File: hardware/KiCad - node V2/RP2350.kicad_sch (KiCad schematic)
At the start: 92 parts, among them J1 Input, J2 Output, J3 USB_C_Receptacle_USB2.0_14P, J4 Screw_Terminal_01x08, SW1 BOOTSEL, U1 RP2350A, U2 THVD1450D, U3 ADXL355BEZ, U4 TPS2121RUXR, U5 USBLC6-2SC6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

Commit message: KiCad: J1 terminal update
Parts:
- removed J1: Input, TerminalBlock_RND:TerminalBlock_RND_205-00278_1x04_P5.00mm_Vertical, symbol Connector:Screw_Terminal_01x04
- removed J2: Output, symbol Connector:Screw_Terminal_01x04
- added C_SHIELD: 10nF, Capacitor_SMD:C_0805_2012Metric, symbol Device:C_Small
- added J1: JST-XH-10, footprints:CONN-TH_10P-P2.50_B10B-XH-A-LF-SN, symbol Connector_Generic:Conn_01x10
- added R_SHIELD: 1M, Resistor_SMD:R_0603_1608Metric, symbol Device:R_Small
- added R_SHIELD_0R: 0R DNP, Resistor_SMD:R_0805_2012Metric, symbol Device:R_Small
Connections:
- net GND: now also C_SHIELD.1, J1.3 (GND_IN), J1.4 (GND_OUT), R_SHIELD.1, R_SHIELD_0R.1
- net at D4.2 (A2), R21.1, U2.6 (A): now also J1.5 (A_IN), J1.7 (A_OUT)
- net at D4.1 (A1), JP1.1 (A), U2.7 (B): now also J1.6 (B_IN), J1.8 (B_OUT)
- net at F1.1: now also J1.1 (12VIN), J1.2 (12VOUT)
- new net: C_SHIELD.2, J1.10 (SH_OUT), J1.9 (SH_IN), R_SHIELD.2, R_SHIELD_0R.2

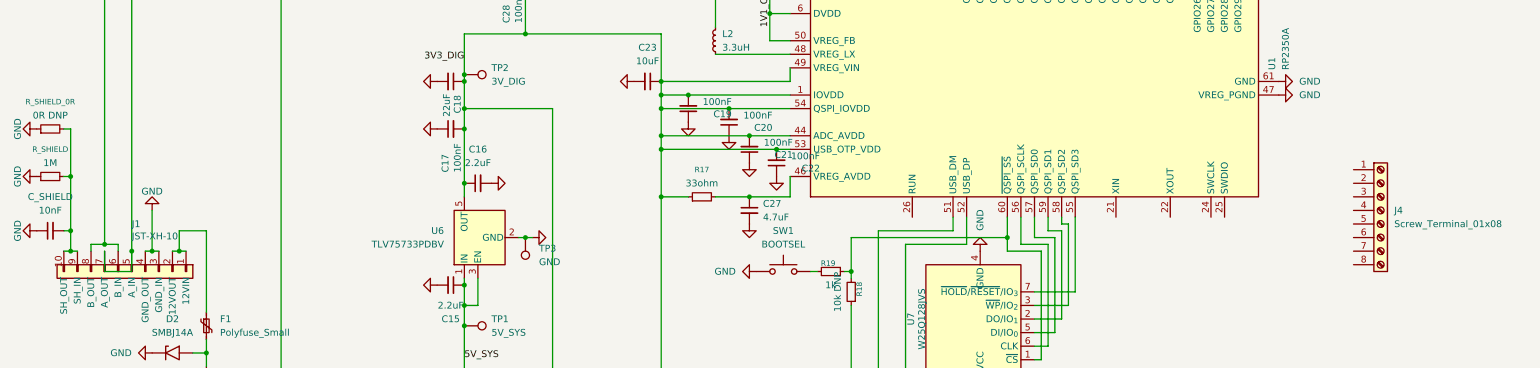
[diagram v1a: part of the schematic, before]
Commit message: hardware: added net classes
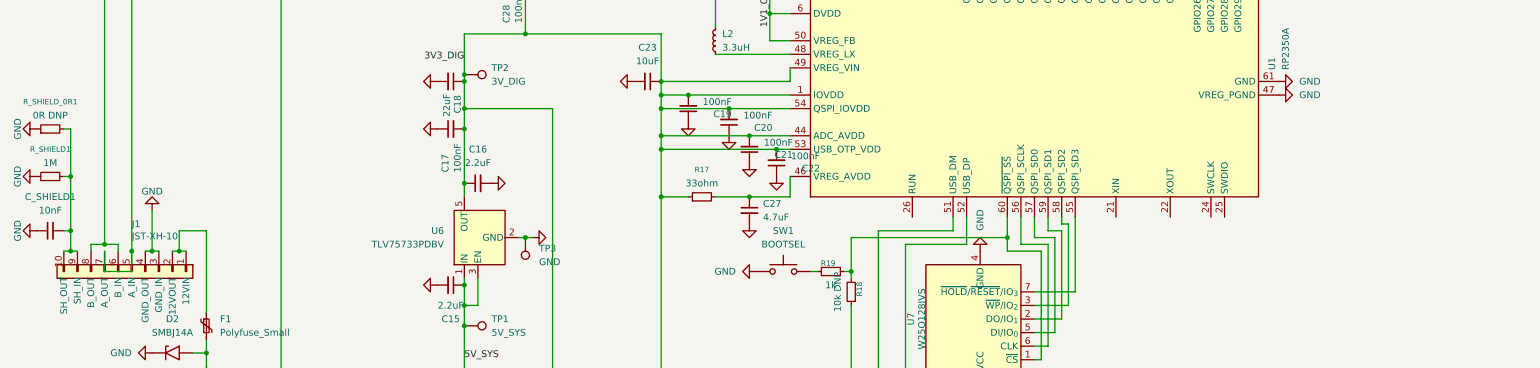
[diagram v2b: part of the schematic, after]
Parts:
- removed J4: Screw_Terminal_01x08, Connector_Molex:Molex_Micro-Fit_3.0_43045-0812_2x04_P3.00mm_Vertical, symbol Connector:Screw_Terminal_01x08
- renumbered C_SHIELD to C_SHIELD1, R_SHIELD to R_SHIELD1, R_SHIELD_0R to R_SHIELD_0R1
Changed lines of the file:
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@@
 		(dnp no)
 		(fields_autoplaced yes)
-		(property "Reference" "R_SHIELD"
+		(property "Reference" "R_SHIELD1"
 			(at 22.86 127 90)
 			(show_name no)
@@
 			(project "RP2350"
 				(path "/e9943aea-ea9d-4269-a668-2289df1fb291"
-					(reference "R_SHIELD")
+					(reference "R_SHIELD1")
 					(unit 1)
 				)
@@
 	)
 	(symbol
-		(lib_id "Connector:Screw_Terminal_01x08")
-		(at 271.78 138.43 0)
-		(unit 1)
-		(body_style 1)
-		(exclude_from_sim no)
-		(in_bom yes)
-		(on_board yes)
-		(in_pos_files yes)
-		(dnp no)
-		(fields_autoplaced yes)
-		(property "Reference" "J4"
-			(at 274.32 138.4299 0)
-			(show_name no)
-			(do_not_autoplace no)
-			(effects
-				(font
-					(size 1.27 1.27)
-				)
-				(justify left)
-			)
-		)
-		(property "Value" "Screw_Terminal_01x08"
-			(at 274.32 140.9699 0)
-			(show_name no)
-			(do_not_autoplace no)
-			(effects
-				(font
-					(size 1.27 1.27)
-				)
-				(justify left)
-			)
-		)
-		(property "Footprint" "Connector_Molex:Molex_Micro-Fit_3.0_43045-0812_2x04_P3.00mm_Vertical"
-			(at 271.78 138.43 0)
-			(hide yes)
-			(show_name no)
-			(do_not_autoplace no)
-			(effects
-				(font
-					(size 1.27 1.27)
-				)
-			)
-		)
-		(property "Datasheet" ""
-			(at 271.78 138.43 0)
-			(hide yes)
-			(show_name no)
-			(do_not_autoplace no)
-			(effects
-				(font
-					(size 1.27 1.27)
-				)
-			)
-		)
-		(property "Description" "Generic screw terminal, single row, 01x08, script generated (kicad-library-utils/schlib/autogen/connector/)"
-			(at 271.78 138.43 0)
-			(hide yes)
-			(show_name no)
-			(do_not_autoplace no)
-			(effects
-				(font
-					(size 1.27 1.27)
-				)
-			)
-		)
-		(pin "5"
-		)
-		(pin "6"
-		)
-		(pin "7"
-		)
-		(pin "8"
-		)
-		(pin "1"
-		)
-		(pin "4"
-		)
-		(pin "2"
-		)
-		(pin "3"
-		)
-		(instances
-			(project "RP2350"
-				(path "/e9943aea-ea9d-4269-a668-2289df1fb291"
-					(reference "J4")
-					(unit 1)
-				)
-			)
-		)
-	)
-	(symbol
 		(lib_id "power:GND")
 		(at 105.41 176.53 90)
@@
 		(dnp no)
 		(fields_autoplaced yes)
-		(property "Reference" "C_SHIELD"
+		(property "Reference" "C_SHIELD1"
 			(at 22.8663 135.89 90)
 			(show_name no)
@@
 			(project "RP2350"
 				(path "/e9943aea-ea9d-4269-a668-2289df1fb291"
-					(reference "C_SHIELD")
+					(reference "C_SHIELD1")
 					(unit 1)
 				)
@@
 		(dnp no)
 		(fields_autoplaced yes)
-		(property "Reference" "R_SHIELD_0R"
+		(property "Reference" "R_SHIELD_0R1"
 			(at 22.86 118.11 90)
 			(show_name no)
@@
 			(project "RP2350"
 				(path "/e9943aea-ea9d-4269-a668-2289df1fb291"
-					(reference "R_SHIELD_0R")
+					(reference "R_SHIELD_0R1")
 					(unit 1)
 				)

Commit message: hardware: 2 terminals fix
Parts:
- removed J1: JST-XH-10, footprints:CONN-TH_10P-P2.50_B10B-XH-A-LF-SN, symbol Connector_Generic:Conn_01x10
- added J_IN1, J_OUT1: JST-GH-5, footprints:CONN-SMD_BM05B-GHS-TBT, symbol Connector_Generic:Conn_01x05
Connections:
- net GND: now also J_IN1.2 (GND), J_OUT1.2 (GND)
- net 12V_BUS: now reaches F1.1
- net 12V_BUS: now also J_IN1.1 (12V), J_OUT1.1 (12V)
- net SHIELD: now reaches C_SHIELD1.2, R_SHIELD1.2, R_SHIELD_0R1.2
- net SHIELD: now also J_IN1.5 (SHIELD), J_OUT1.5 (SHIELD)
- net RS485 A: now reaches D4.2 (A2), R21.1, U2.6 (A)
- net RS485 A: now also J_IN1.3 (A), J_OUT1.3 (A)
- net RS485_B: now reaches D4.1 (A1), JP1.1 (A), U2.7 (B)
- net RS485_B: now also J_IN1.4 (B), J_OUT1.4 (B)
